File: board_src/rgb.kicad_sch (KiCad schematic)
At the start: 8 parts, among them J1 Conn_01x03

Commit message: wersja dodane arkusze hierarchiczne
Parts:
- removed D10: LED, LED_THT:LED_D5.0mm-4_RGB_Wide_Pins, symbol Device:LED
- removed D11, D9: LED, symbol Device:LED
- removed J1: Conn_01x03, Connector_PinHeader_2.00mm:PinHeader_1x03_P2.00mm_Vertical, symbol Connector_Generic:Conn_01x03
- removed R11, R12, R13: 221, Resistor_SMD:R_0201_0603Metric, symbol Device:R
- added J15: Conn_01x03, Connector_PinHeader_2.00mm:PinHeader_1x03_P2.00mm_Vertical, symbol Connector_Generic:Conn_01x03
- added R21, R22, R23: 221, Resistor_SMD:R_0201_0603Metric, symbol Device:R
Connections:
- net +3.3V: now also R21.1, R22.1, R23.1
- net at LED1.1 (K_BLUE): now also J15.3 (Pin_3)
- net at LED1.2 (K_GREEN): now also J15.2 (Pin_2)
- net at LED1.3 (K_RED): now also J15.1 (Pin_1)
- net at LED1.4 (A_RED): now also R23.2
- net at LED1.5 (A_GREEN): now also R22.2
- net at LED1.6 (A_BLUE): now also R21.2
- no-connect marks 6 -> 0
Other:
- note removed: "RGB"
- moved on the sheet: LED1

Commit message: wersja uzupelnione footprinty
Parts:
- J15: footprint Connector_PinHeader_2.00mm:PinHeader_1x03_P2.00mm_Vertical -> Connector_PinHeader_2.54mm:PinHeader_1x03_P2.54mm_Vertical
- LED1: footprint ASMT-YTC7-0AA02 -> footprints:ASMT-YTC7-0AA02
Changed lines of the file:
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@@
 			)
 		)
-		(property "Footprint" "Connector_PinHeader_2.00mm:PinHeader_1x03_P2.00mm_Vertical"
+		(property "Footprint" "Connector_PinHeader_2.54mm:PinHeader_1x03_P2.54mm_Vertical"
 			(at 199.39 95.25 0)
 			(effects
@@
 			)
 		)
-		(property "Footprint" "ASMT-YTC7-0AA02"
+		(property "Footprint" "footprints:ASMT-YTC7-0AA02"
 			(at 185.42 187.63 0)
 			(effects

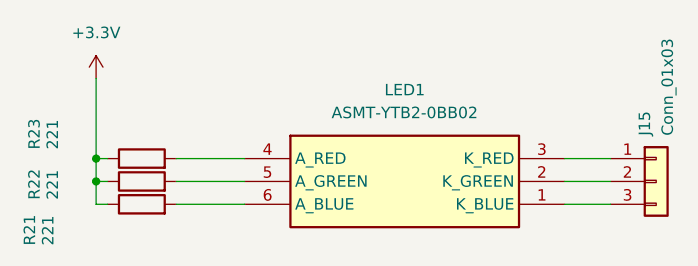
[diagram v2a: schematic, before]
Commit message: wersja z wyswietlaczem LCD
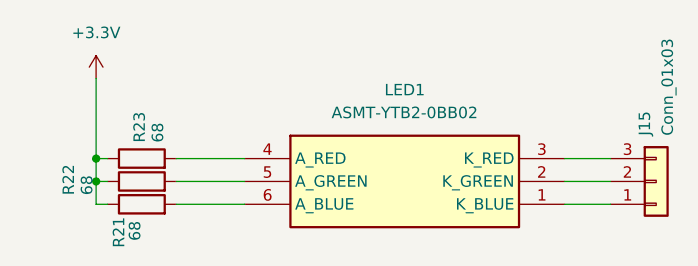
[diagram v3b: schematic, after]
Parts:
- R21, R22, R23: value 221 -> 68
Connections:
- net at J15.1 (Pin_3): now also LED1.1 (K_BLUE); no longer LED1.3 (K_RED)
- net at J15.3 (Pin_1): now also LED1.3 (K_RED); no longer LED1.1 (K_BLUE)
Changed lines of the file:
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@@
 		(dnp no)
 		(property "Reference" "R22"
-			(at 130.302 97.282 0)
-			(effects
-				(font
-					(size 1.27 1.27)
-				)
-				(justify left)
-			)
-		)
-		(property "Value" "221"
-			(at 132.334 97.282 0)
+			(at 134.112 96.774 0)
+			(effects
+				(font
+					(size 1.27 1.27)
+				)
+				(justify left)
+			)
+		)
+		(property "Value" "68"
+			(at 136.144 96.774 0)
 			(effects
 				(font
@@
 		(dnp no)
 		(property "Reference" "R21"
-			(at 129.794 102.362 0)
-			(effects
-				(font
-					(size 1.27 1.27)
-				)
-				(justify left)
-			)
-		)
-		(property "Value" "221"
-			(at 131.826 102.362 0)
+			(at 139.7 102.616 0)
+			(effects
+				(font
+					(size 1.27 1.27)
+				)
+				(justify left)
+			)
+		)
+		(property "Value" "68"
+			(at 141.478 101.854 0)
 			(effects
 				(font
@@
 		(dnp no)
 		(property "Reference" "R23"
-			(at 130.302 91.694 0)
-			(effects
-				(font
-					(size 1.27 1.27)
-				)
-				(justify left)
-			)
-		)
-		(property "Value" "221"
-			(at 132.334 91.694 0)
-			(effects
-				(font
+			(at 141.986 90.932 0)
+			(effects
+				(font
+					(size 1.27 1.27)
+				)
+				(justify left)
+			)
+		)
+		(property "Value" "68"
+			(at 144.018 90.932 0)
+			(effects
+				(font

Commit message: wersja z FT232RN
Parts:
- R21, R22, R23: footprint Resistor_SMD:R_0201_0603Metric -> Resistor_SMD:R_1206_3216Metric
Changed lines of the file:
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@@
 			)
 		)
-		(property "Footprint" "Resistor_SMD:R_0201_0603Metric"
+		(property "Footprint" "Resistor_SMD:R_1206_3216Metric"
 			(at 142.24 97.028 90)
 			(effects
@@
 			)
 		)
-		(property "Footprint" "Resistor_SMD:R_0201_0603Metric"
+		(property "Footprint" "Resistor_SMD:R_1206_3216Metric"
 			(at 142.24 99.568 90)
 			(effects
@@
 			)
 		)
-		(property "Footprint" "Resistor_SMD:R_0201_0603Metric"
+		(property "Footprint" "Resistor_SMD:R_1206_3216Metric"
 			(at 142.24 94.488 90)
 			(effects

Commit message: Wersja ze sciezkami miedzianymi
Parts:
- R21, R22, R23: footprint Resistor_SMD:R_1206_3216Metric -> Resistor_SMD:R_0603_1608Metric
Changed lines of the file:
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@@
 			)
 		)
-		(property "Footprint" "Resistor_SMD:R_1206_3216Metric"
+		(property "Footprint" "Resistor_SMD:R_0603_1608Metric"
 			(at 142.24 97.028 90)
 			(effects
@@
 			)
 		)
-		(property "Footprint" "Resistor_SMD:R_1206_3216Metric"
+		(property "Footprint" "Resistor_SMD:R_0603_1608Metric"
 			(at 142.24 99.568 90)
 			(effects
@@
 			)
 		)
-		(property "Footprint" "Resistor_SMD:R_1206_3216Metric"
+		(property "Footprint" "Resistor_SMD:R_0603_1608Metric"
 			(at 142.24 94.488 90)
 			(effects

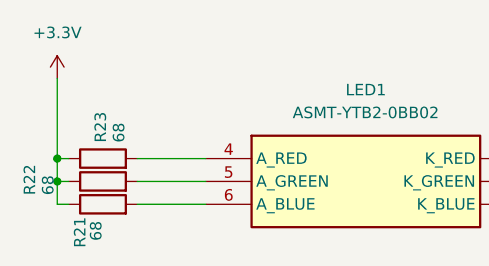
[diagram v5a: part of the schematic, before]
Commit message: poprawione polaczenia diod i wartosci opornikow, aktualizacja niektorych elementow ze wzgledu na braki w magazynie
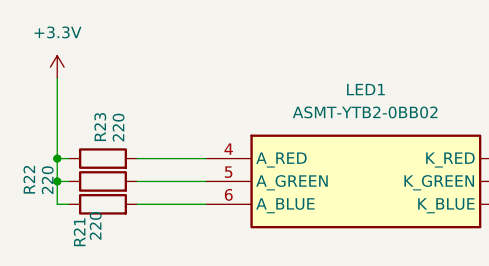
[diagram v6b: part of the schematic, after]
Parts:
- R21, R22, R23: value 68 -> 220
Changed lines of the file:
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@@
 			)
 		)
-		(property "Value" "68"
+		(property "Value" "220"
 			(at 136.144 96.774 0)
 			(effects
@@
 			)
 		)
-		(property "Value" "68"
+		(property "Value" "220"
 			(at 141.478 101.854 0)
 			(effects
@@
 			)
 		)
-		(property "Value" "68"
+		(property "Value" "220"
 			(at 144.018 90.932 0)
 			(effects

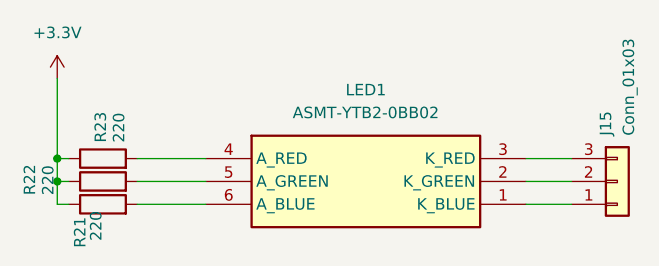
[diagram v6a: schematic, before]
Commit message: Poprawki w schematach. Rozpoczęte korekty płytki
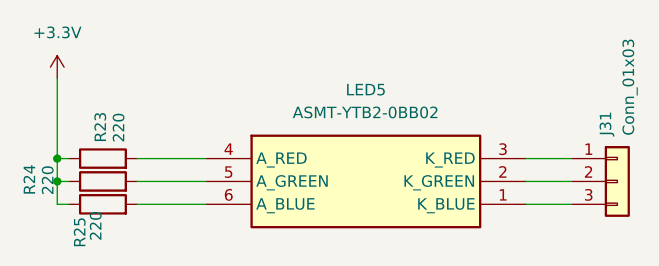
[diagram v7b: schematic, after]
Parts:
- J31: renamed from J15; footprint Connector_PinHeader_2.54mm:PinHeader_1x03_P2.54mm_Vertical -> Connector_PinHeader_2.54mm:PinHeader_1x10_P2.54mm_Vertical
- LED5: renamed from LED1; footprint footprints:ASMT-YTC7-0AA02 -> LED_SMD:LED_0603_1608Metric_Pad1.05x0.95mm_HandSolder
- R23: footprint Resistor_SMD:R_0603_1608Metric -> Resistor_SMD:R_0603_1608Metric_Pad0.98x0.95mm_HandSolder
- R24: renamed from R22; footprint Resistor_SMD:R_0603_1608Metric -> Resistor_SMD:R_0603_1608Metric_Pad0.98x0.95mm_HandSolder
- R25: renamed from R21; footprint Resistor_SMD:R_0603_1608Metric -> Resistor_SMD:R_0603_1608Metric_Pad0.98x0.95mm_HandSolder
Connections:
- net at J31.1 (Pin_1): now also LED5.3 (K_RED); no longer LED5.1 (K_BLUE)
- net at J31.3 (Pin_3): now also LED5.1 (K_BLUE); no longer LED5.3 (K_RED)
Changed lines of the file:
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@@
 		(on_board yes)
 		(dnp no)
-		(property "Reference" "R22"
+		(property "Reference" "R24"
 			(at 134.112 96.774 0)
 			(effects
@@
 			)
 		)
-		(property "Footprint" "Resistor_SMD:R_0603_1608Metric"
+		(property "Footprint" "Resistor_SMD:R_0603_1608Metric_Pad0.98x0.95mm_HandSolder"
 			(at 142.24 97.028 90)
 			(effects
@@
 			(project "board"
 				(path "/772e9f49-cfcf-4cf6-843d-0684684f2d4b/2ad7fc0c-38f7-4b2f-bd87-4c3b79aeda46"
-					(reference "R22")
+					(reference "R24")
 					(unit 1)
 				)
@@
 		(dnp no)
 		(fields_autoplaced yes)
-		(property "Reference" "J15"
+		(property "Reference" "J31"
 			(at 198.1199 90.17 90)
 			(effects
@@
 			)
 		)
-		(property "Footprint" "Connector_PinHeader_2.54mm:PinHeader_1x03_P2.54mm_Vertical"
+		(property "Footprint" "Connector_PinHeader_2.54mm:PinHeader_1x10_P2.54mm_Vertical"
 			(at 199.39 95.25 0)
 			(effects
@@
 			(project "board"
 				(path "/772e9f49-cfcf-4cf6-843d-0684684f2d4b/2ad7fc0c-38f7-4b2f-bd87-4c3b79aeda46"
-					(reference "J15")
+					(reference "J31")
 					(unit 1)
 				)
@@
 		(on_board yes)
 		(dnp no)
-		(property "Reference" "R21"
+		(property "Reference" "R25"
 			(at 139.7 102.616 0)
 			(effects
@@
 			)
 		)
-		(property "Footprint" "Resistor_SMD:R_0603_1608Metric"
+		(property "Footprint" "Resistor_SMD:R_0603_1608Metric_Pad0.98x0.95mm_HandSolder"
 			(at 142.24 99.568 90)
 			(effects
@@
 			(project "board"
 				(path "/772e9f49-cfcf-4cf6-843d-0684684f2d4b/2ad7fc0c-38f7-4b2f-bd87-4c3b79aeda46"
-					(reference "R21")
+					(reference "R25")
 					(unit 1)
 				)
@@
 		(dnp no)
 		(fields_autoplaced yes)
-		(property "Reference" "#PWR028"
+		(property "Reference" "#PWR058"
 			(at 137.16 87.63 0)
 			(effects
@@
 			(project "board"
 				(path "/772e9f49-cfcf-4cf6-843d-0684684f2d4b/2ad7fc0c-38f7-4b2f-bd87-4c3b79aeda46"
-					(reference "#PWR028")
+					(reference "#PWR058")
 					(unit 1)
 				)
@@
 			)
 		)
-		(property "Footprint" "Resistor_SMD:R_0603_1608Metric"
+		(property "Footprint" "Resistor_SMD:R_0603_1608Metric_Pad0.98x0.95mm_HandSolder"
 			(at 142.24 94.488 90)
 			(effects
@@
 		(dnp no)
 		(fields_autoplaced yes)
-		(property "Reference" "LED1"
+		(property "Reference" "LED5"
 			(at 171.45 85.09 0)
 			(effects
@@
 			)
 		)
-		(property "Footprint" "footprints:ASMT-YTC7-0AA02"
+		(property "Footprint" "LED_SMD:LED_0603_1608Metric_Pad1.05x0.95mm_HandSolder"
 			(at 185.42 187.63 0)
 			(effects
@@
 			(project ""
 				(path "/772e9f49-cfcf-4cf6-843d-0684684f2d4b/2ad7fc0c-38f7-4b2f-bd87-4c3b79aeda46"
-					(reference "LED1")
-					(unit 1)
-				)
+					(reference "LED5")
+					(unit 1)
+				)

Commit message: Naniesione poprawki na projekcie płytki. Wersja końcowa
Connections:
- net at J31.1 (Pin_1): now also LED5.1 (K_BLUE); no longer LED5.3 (K_RED)
- net at J31.3 (Pin_3): now also LED5.3 (K_RED); no longer LED5.1 (K_BLUE)
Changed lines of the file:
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@@
 		(lib_id "Connector_Generic:Conn_01x03")
 		(at 199.39 95.25 0)
+		(mirror x)
 		(unit 1)
 		(exclude_from_sim no)
@@
 		(on_board yes)
 		(dnp no)
-		(fields_autoplaced yes)
 		(property "Reference" "J31"
-			(at 198.1199 90.17 90)
+			(at 199.39 86.36 0)
 			(effects
 				(font
 					(size 1.27 1.27)
 				)
-				(justify left)
 			)
 		)
 		(property "Value" "Conn_01x03"
-			(at 200.6599 90.17 90)
+			(at 199.39 88.9 0)
 			(effects
 				(font
 					(size 1.27 1.27)
 				)
-				(justify left)
 			)
 		)
